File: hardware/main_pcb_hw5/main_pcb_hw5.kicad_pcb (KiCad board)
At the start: 2 copper layers, 100 x 100 mm, 27 parts, among them J1 MEGA TOP, J10 GBA_Slot, J2 MEGA BOTTOM, J3 CART SLOT TOP ROW, J4 CART SLOT BOTTOM ROW, J5 MEGA SIDE, J6 5V USB, J7 Conn_01x07, J8 EXP2, J9 EXP1, M2_1 Screw_Terminal_01x01, M2_2 Screw_Terminal_01x01, M2_3 Screw_Terminal_01x01, M2_4 Screw_Terminal_01x01, M2_5 Screw_Terminal_01x01, M2_6 Screw_Terminal_01x01, M2_7 Screw_Terminal_01x01, M2_8 Screw_Terminal_01x01, M2_9 Screw_Terminal_01x01, SW1 VOLTAGE, SW2 POWER

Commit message: Update silkscreen
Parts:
- JP2: value powered by 5V -> Testpoints 1 2
- JP3: value 3V3 from Arduino -> Testpoints 3 4
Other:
- board text added: "J1"
- board text added: "J2"
- board text added: "TP1"
- board text added: "TP2"
- board text added: "TP3"
- board text added: "TP4"
- board text removed: "powered by 5V"
- board text removed: "powered by VCC"
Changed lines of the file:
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@@
       (effects (font (size 1 1) (thickness 0.15)) (justify mirror))
     )
-    (fp_text value "powered by 5V" (at 5.01 -2.34 180 unlocked) (layer "B.SilkS") hide
+    (fp_text value "Testpoints 1 2" (at 5.01 -2.34 180 unlocked) (layer "B.SilkS") hide
       (effects (font (size 0.7 0.7) (thickness 0.15)) (justify left mirror))
     )
-    (fp_line (start -1.4 -1) (end -1.4 1) (layer "B.SilkS") (width 0.12))
-    (fp_line (start -1.4 1) (end 1.4 1) (layer "B.SilkS") (width 0.12))
-    (fp_line (start 1.4 1) (end 1.4 -1) (layer "B.SilkS") (width 0.12))
-    (fp_line (start 1.4 -1) (end -1.4 -1) (layer "B.SilkS") (width 0.12))
     (fp_line (start -1.65 1.25) (end 1.65 1.25) (layer "B.CrtYd") (width 0.05))
     (fp_line (start -1.65 1.25) (end -1.65 -1.25) (layer "B.CrtYd") (width 0.05))
     (fp_line (start 1.65 -1.25) (end -1.65 -1.25) (layer "B.CrtYd") (width 0.05))
     (fp_line (start 1.65 -1.25) (end 1.65 1.25) (layer "B.CrtYd") (width 0.05))
-    (pad "1" smd rect locked (at -0.65 0 180) (size 1 1.5) (layers "B.Cu" "B.Mask")
+    (pad "1" smd rect (at -0.65 0 180) (size 1 1.5) (layers "B.Cu" "B.Mask")
       (net 72 "+5V") (pinfunction "A") (pintype "passive"))
-    (pad "2" smd rect locked (at 0.65 0 180) (size 1 1.5) (layers "B.Cu" "B.Mask")
+    (pad "2" smd rect (at 0.65 0 180) (size 1 1.5) (layers "B.Cu" "B.Mask")
       (net 92 "VDDA") (pinfunction "B") (pintype "passive"))
   )
@@
       (effects (font (size 1 1) (thickness 0.15)) (justify mirror))
     )
-    (fp_text value "3V3 from Arduino" (at 11 0 180 unlocked) (layer "B.SilkS") hide
+    (fp_text value "Testpoints 3 4" (at 11 0 180 unlocked) (layer "B.SilkS") hide
       (effects (font (size 0.7 0.7) (thickness 0.15)) (justify left mirror))
     )
-    (fp_line (start -1.4 -1) (end -1.4 1) (layer "B.SilkS") (width 0.12))
-    (fp_line (start -1.4 1) (end 1.4 1) (layer "B.SilkS") (width 0.12))
-    (fp_line (start 1.4 -1) (end -1.4 -1) (layer "B.SilkS") (width 0.12))
-    (fp_line (start 1.4 1) (end 1.4 -1) (layer "B.SilkS") (width 0.12))
+    (fp_line (start 1.65 -1.25) (end -1.65 -1.25) (layer "B.CrtYd") (width 0.05))
+    (fp_line (start -1.65 1.25) (end -1.65 -1.25) (layer "B.CrtYd") (width 0.05))
+    (fp_line (start -1.65 1.25) (end 1.65 1.25) (layer "B.CrtYd") (width 0.05))
     (fp_line (start 1.65 -1.25) (end 1.65 1.25) (layer "B.CrtYd") (width 0.05))
-    (fp_line (start -1.65 1.25) (end 1.65 1.25) (layer "B.CrtYd") (width 0.05))
-    (fp_line (start -1.65 1.25) (end -1.65 -1.25) (layer "B.CrtYd") (width 0.05))
-    (fp_line (start 1.65 -1.25) (end -1.65 -1.25) (layer "B.CrtYd") (width 0.05))
-    (pad "1" smd rect locked (at -0.65 0 180) (size 1 1.5) (layers "B.Cu" "B.Mask")
+    (pad "1" smd rect (at -0.65 0 180) (size 1 1.5) (layers "B.Cu" "B.Mask")
       (net 35 "+3.3VA") (pinfunction "A") (pintype "passive"))
-    (pad "2" smd rect locked (at 0.65 0 180) (size 1 1.5) (layers "B.Cu" "B.Mask")
+    (pad "2" smd rect (at 0.65 0 180) (size 1 1.5) (layers "B.Cu" "B.Mask")
       (net 71 "+3V3") (pinfunction "B") (pintype "passive"))
   )
@@
   (gr_line (start 152.9063 146.1343) (end 152.8131 146.0411) (layer "B.SilkS") (width 0.1))
   (gr_line (start 138.7022 113.3433) (end 138.8887 113.3433) (layer "B.SilkS") (width 0.1))
-  (gr_line (start 169.21 123.505) (end 167.7 123.505) (layer "B.SilkS") (width 0.15))
   (gr_line (start 153.7874 143.5362) (end 154.1602 143.9091) (layer "B.SilkS") (width 0.1))
   (gr_line (start 154.1633 115.9735) (end 153.9769 115.9735) (layer "B.SilkS") (width 0.1))
@@
   (gr_line (start 110.97 115.68785) (end 110.5972 115.68785) (layer "B.SilkS") (width 0.1))
   (gr_line (start 152.9471 115.9735) (end 153.0403 115.8803) (layer "B.SilkS") (width 0.1))
-  (gr_line (start 170.35 121.43) (end 169.21 121.43) (layer "B.SilkS") (width 0.15))
   (gr_line (start 138.2671 115.4142) (end 137.8943 115.4142) (layer "B.SilkS") (width 0.1))
   (gr_line (start 115.2019 115.8836) (end 115.1087 115.9768) (layer "B.SilkS") (width 0.1))
@@
   (gr_line (start 132.6556 115.8803) (end 132.6556 115.5075) (layer "B.SilkS") (width 0.1))
   (gr_line (start 123.3135 146.0411) (end 123.1271 146.0411) (layer "B.SilkS") (width 0.1))
-  (gr_line (start 107.421 116.57) (end 107.611 116.81) (layer "B.SilkS") (width 0.15))
   (gr_line (start 143.8333 113.0637) (end 143.9265 113.0637) (layer "B.SilkS") (width 0.1))
   (gr_line (start 109.7534 113.33285) (end 109.567 113.33285) (layer "B.SilkS") (width 0.1))
@@
   (gr_line (start 117.6676 115.8803) (end 117.6676 115.5075) (layer "B.SilkS") (width 0.1))
   (gr_line (start 144.8851 143.9989) (end 145.1647 143.9989) (layer "B.SilkS") (width 0.1))
-  (gr_line (start 153.5 123.505) (end 107.42 123.505) (layer "B.SilkS") (width 0.15))
   (gr_line (start 146.4741 143.4397) (end 146.1013 143.4397) (layer "B.SilkS") (width 0.1))
   (gr_line (start 149.1178 115.5075) (end 149.0246 115.4142) (layer "B.SilkS") (width 0.1))
@@
   (gr_line (start 149.4548 138.1125) (end 150.0141 138.1125) (layer "B.SilkS") (width 0.1))
   (gr_line (start 133.778599 115.9735) (end 133.778599 115.4142) (layer "B.SilkS") (width 0.1))
-  (gr_line (start 169.21 125.58) (end 170.35 125.58) (layer "B.SilkS") (width 0.15))
   (gr_line (start 133.6005 113.1569) (end 133.414 113.0637) (layer "B.SilkS") (width 0.1))
   (gr_line (start 140.8546 146.414) (end 140.8546 146.5072) (layer "B.SilkS") (width 0.1))
@@
   (gr_line (start 138.8214 146.3208) (end 138.4485 146.3208) (layer "B.SilkS") (width 0.1))
   (gr_line (start 136.1541 143.9989) (end 135.9677 143.9989) (layer "B.SilkS") (width 0.1))
-  (gr_line (start 169.21 121.43) (end 169.21 125.58) (layer "B.SilkS") (width 0.15))
   (gr_line (start 140.1535 115.9735) (end 140.2467 115.8803) (layer "B.SilkS") (width 0.1))
   (gr_line (start 149.548 136.8963) (end 149.4548 136.8031) (layer "B.SilkS") (width 0.1))
@@
   (gr_line (start 147.4984 146.6004) (end 147.7781 146.6004) (layer "B.SilkS") (width 0.1))
   (gr_line (start 138.2133 146.1343) (end 138.2133 146.2276) (layer "B.SilkS") (width 0.1))
-  (gr_line (start 107.42 123.5) (end 107.42 116.57) (layer "B.SilkS") (width 0.15))
   (gr_line (start 135.6452 115.4142) (end 135.6452 115.9735) (layer "B.SilkS") (width 0.1))
   (gr_line (start 120.1343 112.7874) (end 119.8547 112.7874) (layer "B.SilkS") (width 0.1))
@@
   (gr_line (start 153.5552 115.4142) (end 153.6484 115.5075) (layer "B.SilkS") (width 0.1))
   (gr_line (start 134.6583 143.4397) (end 134.6583 143.9989) (layer "B.SilkS") (width 0.1))
-  (gr_line (start 107.421 116.57) (end 107.241 116.8) (layer "B.SilkS") (width 0.15))
   (gr_line (start 131.0464 143.4397) (end 131.1396 143.5329) (layer "B.SilkS") (width 0.1))
   (gr_line (start 120.5141 146.3241) (end 120.7937 146.6037) (layer "B.SilkS") (width 0.1))
@@
     (effects (font (size 0.7 0.7) (thickness 0.125)) (justify left mirror))
   )
+  (gr_text "TP2" (at 182.7 129 90) (layer "B.SilkS")
+    (effects (font (size 0.7 0.7) (thickness 0.125)) (justify right mirror))
+  )
   (gr_text "D4" (at 125.58 99.345 90) (layer "B.SilkS")
     (effects (font (size 0.7 0.7) (thickness 0.125)) (justify left mirror))
@@
     (effects (font (size 0.7 0.7) (thickness 0.125)) (justify left mirror))
   )
+  (gr_text "TP1" (at 181.4 129 90) (layer "B.SilkS")
+    (effects (font (size 0.7 0.7) (thickness 0.125)) (justify right mirror))
+  )
   (gr_text "D50" (at 194 83.935 90) (layer "B.SilkS")
     (effects (font (size 0.7 0.7) (thickness 0.125)) (justify left mirror))
@@
     (effects (font (size 0.7 0.7) (thickness 0.15)) (justify mirror))
   )
-  (gr_text "powered by 5V" (at 171.01 125.66 180) (layer "B.SilkS")
-    (effects (font (size 0.7 0.7) (thickness 0.125)) (justify left mirror))
-  )
   (gr_text "CLK1" (at 181.3 99.345 90) (layer "B.SilkS")
     (effects (font (size 0.7 0.7) (thickness 0.125)) (justify left mirror))
@@
     (effects (font (size 0.7 0.7) (thickness 0.125)) (justify left mirror))
   )
-  (gr_text "MEGA 2560 PRO" (at 154.24 123.5 180) (layer "B.SilkS")
-    (effects (font (size 1 1) (thickness 0.15)) (justify left mirror))
-  )
   (gr_text "CLK0" (at 181.3 114.415 180) (layer "B.SilkS")
     (effects (font (size 0.6 0.6) (thickness 0.15)) (justify mirror))
@@
     (effects (font (size 0.7 0.7) (thickness 0.125)) (justify left mirror))
   )
+  (gr_text "J1" (at 182.7 119.7 180) (layer "B.SilkS")
+    (effects (font (size 0.7 0.7) (thickness 0.125)) (justify right mirror))
+  )
   (gr_text "A12" (at 140.68 84.055 90) (layer "B.SilkS")
     (effects (font (size 0.7 0.7) (thickness 0.125)) (justify left mirror))
+  )
+  (gr_text "J2" (at 186.5 119.7 180) (layer "B.SilkS")
+    (effects (font (size 0.7 0.7) (thickness 0.125)) (justify right mirror))
   )
   (gr_text "D26" (at 143.36 99.345 90) (layer "B.SilkS")
@@
     (effects (font (size 0.7 0.7) (thickness 0.125)) (justify left mirror))
   )
+  (gr_text "TP3" (at 185.2 129 90) (layer "B.SilkS")
+    (effects (font (size 0.7 0.7) (thickness 0.125)) (justify right mirror))
+  )
   (gr_text "D28" (at 148.44 99.345 90) (layer "B.SilkS")
     (effects (font (size 0.7 0.7) (thickness 0.125)) (justify left mirror))
@@
     (effects (font (size 0.7 0.7) (thickness 0.125)) (justify left mirror))
   )
-  (gr_text "powered by VCC" (at 171.01 121.66 180) (layer "B.SilkS")
-    (effects (font (size 0.7 0.7) (thickness 0.125)) (justify left mirror))
-  )
   (gr_text "GND" (at 196.54 83.935 90) (layer "B.SilkS")
     (effects (font (size 0.7 0.7) (thickness 0.125)) (justify left mirror))
@@
     (effects (font (size 0.7 0.7) (thickness 0.125)) (justify left mirror))
   )
+  (gr_text "TP4" (at 186.6 129 90) (layer "B.SilkS")
+    (effects (font (size 0.7 0.7) (thickness 0.125)) (justify right mirror))
+  )
   (gr_text "D16" (at 173.7 84.055 90) (layer "B.SilkS")

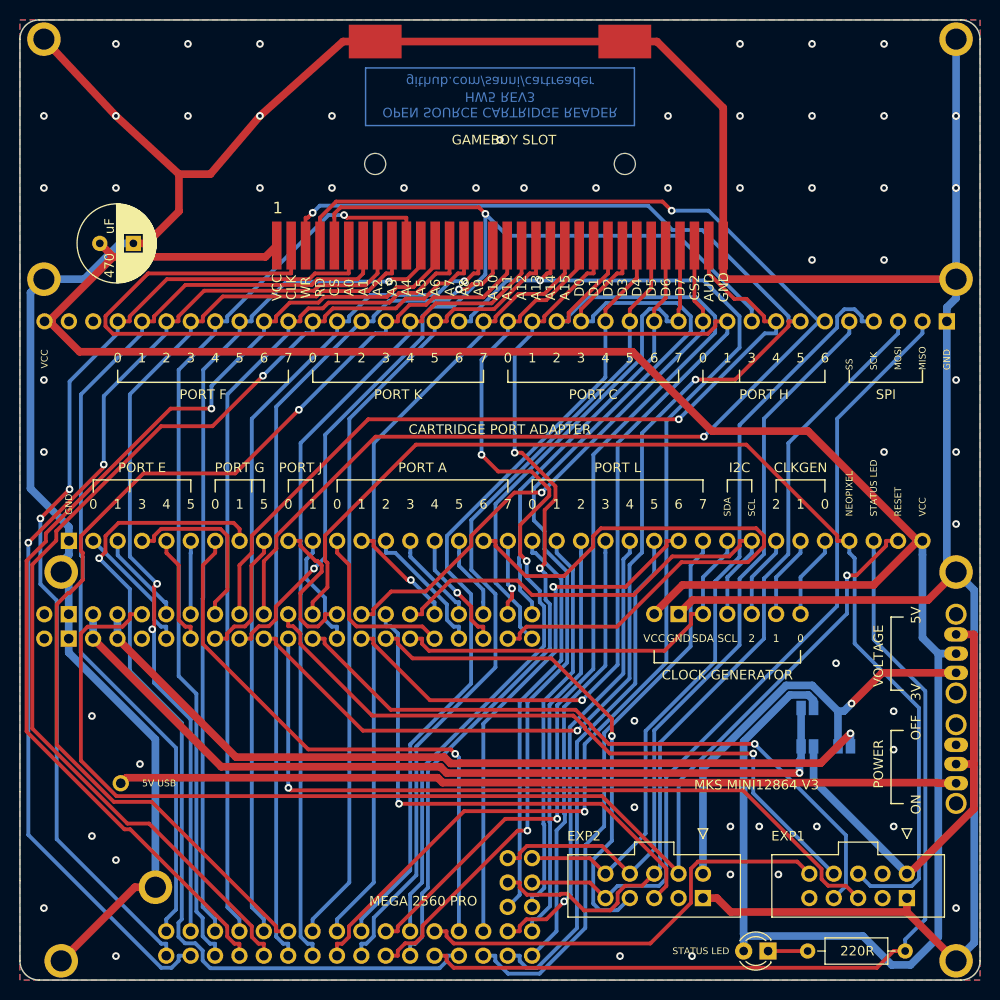
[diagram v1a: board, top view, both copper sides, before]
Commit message: New OSCR Logo + Vselect built into main PCB
Also added symbol and footprint library links
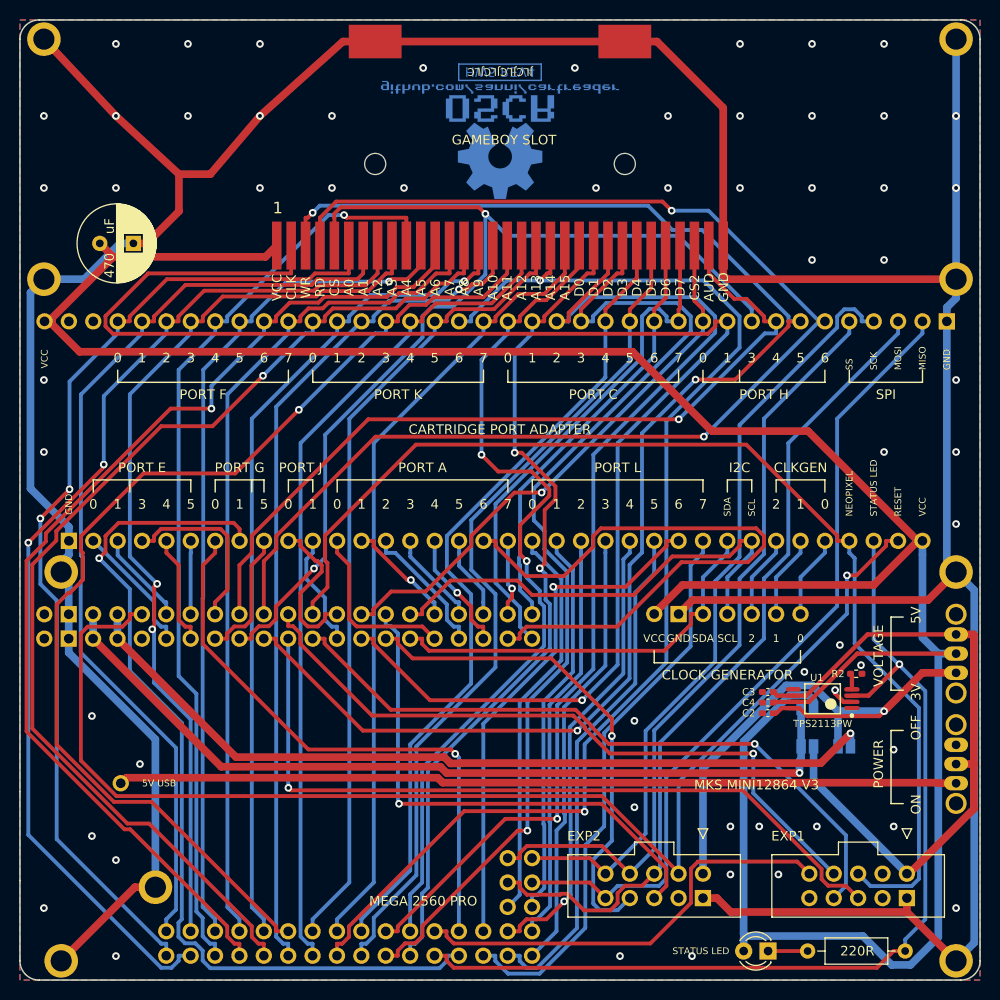
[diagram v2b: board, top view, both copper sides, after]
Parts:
- added C2: 0.1 uF, Capacitor_SMD:C_0402_1005Metric_Pad0.74x0.62mm_HandSolder, F.Cu at (177.9, 122.2)
- added C3: 0.1 uF, Capacitor_SMD:C_0402_1005Metric_Pad0.74x0.62mm_HandSolder, F.Cu at (177.9, 120.0)
- added C4: 10 uF, Capacitor_SMD:C_0402_1005Metric_Pad0.74x0.62mm_HandSolder, F.Cu at (177.9, 121.1)
- added G***: LOGO, !OSCR:Logo, B.Cu at (150.0, 62.5)
- added R2: 550, Resistor_SMD:R_0402_1005Metric_Pad0.72x0.64mm_HandSolder, F.Cu at (187.1, 118.1)
- added U1: TPS2113PW, Personal:Texas_Instruments-TPS2113PW-Level_A, F.Cu at (183.6, 120.7)
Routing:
- net +5V: track 48.9 -> 70.8 mm
- net VCC: track 259.2 -> 280.4 mm
- net +3V3: track 47.3 -> 59.6 mm
- net D38: track 96.4 -> 102.8 mm, vias 0 -> 1
- net GND: track 390.5 -> 392.9 mm, vias 58 -> 59
- net Net-(R2-Pad2): track 0.00 -> 1.69 mm
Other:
- board text added: "HW5 REV4"
- board text added: "JLCJLCJLCJLC"
- board text removed: "OPEN SOURCE CARTRIDGE READER HW5 REV3 github.com/sanni/cartreader"

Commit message: HW5 Main PCB, Revision 5
* Migrated files to KiCad 7
* Added RTC
  * IC: Analog Devices Inc. DS3231MZ
  * Battery holder (CR1616): Keystone Electronics 3012
* Cleaned up traces
* Changed ground fill to solid
* Removed test pads and LCD solder jumper
* Cleaned up/prettified silkscreen and logo
* Cleaned up some footprints (more to come eventually)
* Added 3D models for board display
* Schematic image is now a PDF since it has 2 pages
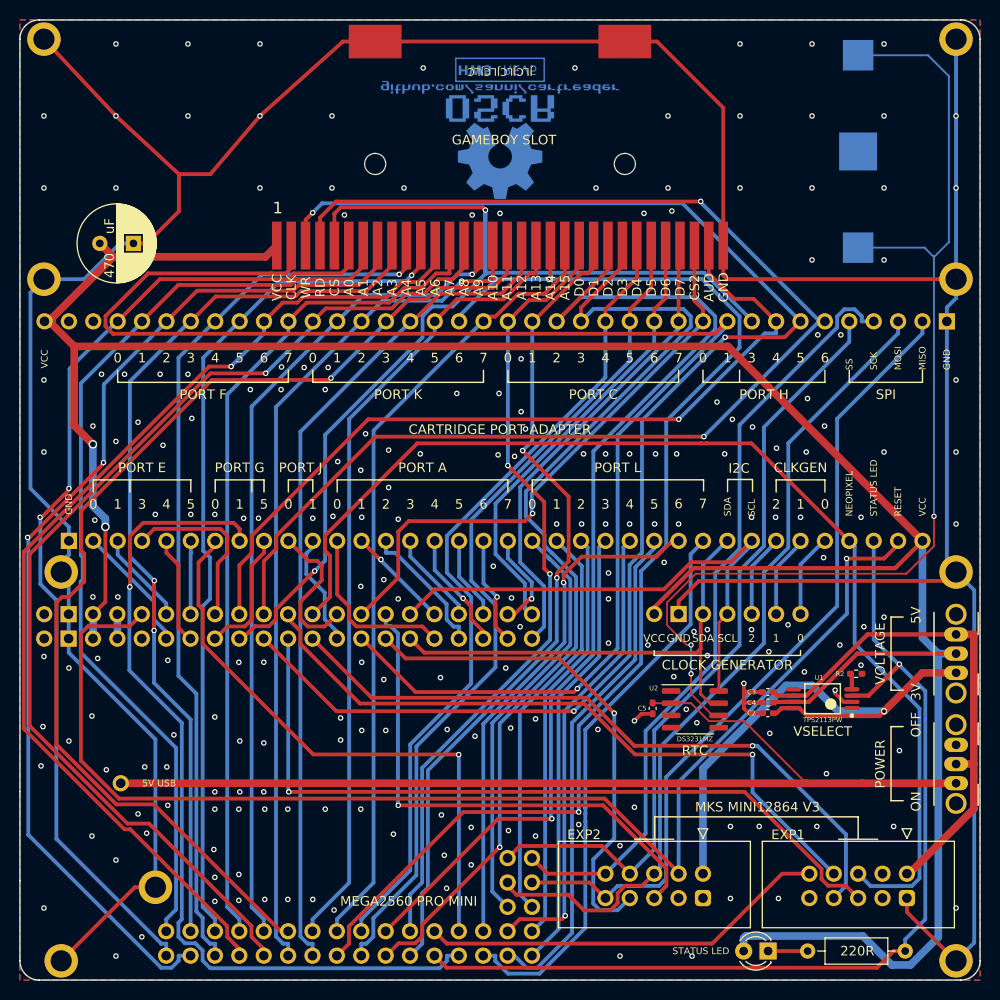
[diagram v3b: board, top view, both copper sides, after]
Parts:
- removed J2: MEGA BOTTOM, Connector_PinSocket_2.54mm:PinSocket_2x16_P2.54mm_Vertical
- removed J5: MEGA SIDE, Connector_PinSocket_2.54mm:PinSocket_2x03_P2.54mm_Vertical
- removed JP1: powered by VCC, Jumper:SolderJumper-2_P1.3mm_Open_Pad1.0x1.5mm
- removed JP2: Testpoints 1 2, Jumper:SolderJumper-2_P1.3mm_Open_Pad1.0x1.5mm
- removed JP3: Testpoints 3 4, Jumper:SolderJumper-2_P1.3mm_Open_Pad1.0x1.5mm
- added BT1: CR1616, !OSCR:CR1616, B.Cu at (187.3, 63.7)
- added C5: 0.1u, Capacitor_SMD:C_0402_1005Metric_Pad0.74x0.62mm_HandSolder, F.Cu at (165.9, 121.7)
- added U2: DS3231MZ, Package_SO:SOIC-8_3.9x4.9mm_P1.27mm, F.Cu at (170.3, 121.8)
- C1: value C_Polarized -> 470u
- C2, C3: value 0.1 uF -> 0.1u
- C4: value 10 uF -> 10u
- J1: value MEGA TOP -> MEGA BOTTOM; footprint Connector_PinSocket_2.54mm:PinSocket_2x21_P2.54mm_Vertical -> !OSCR:MEGA2560_PRO_MINI
- J3: footprint Connector_PinSocket_2.54mm:PinSocket_1x38_P2.54mm_Vertical -> !OSCR:Cartridge_Port_Adapter-Back
- J4: value CART SLOT BOTTOM ROW -> CART SLOT FRONT ROW; footprint Connector_PinSocket_2.54mm:PinSocket_1x36_P2.54mm_Vertical -> !OSCR:Cartridge_Port_Adapter-Front
- J7: footprint Connector_PinHeader_2.54mm:PinHeader_1x07_P2.54mm_Vertical -> !OSCR:Clock_Generator_Header
- J8, J9: footprint Connector_IDC:IDC-Header_2x05_P2.54mm_Vertical -> !OSCR:LCD_Header
- R2: value 550 -> 560R
- SW1, SW2: footprint Button_Switch_THT:SW_CuK_OS102011MA1QN1_SPDT_Angled -> !OSCR:Power_Switch
- moved J1 25.4 mm to (127.9, 113.0), turned to 0 degrees
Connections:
- J1 pad 37: VDDA -> VCC
- J1 pad 38: VDDA -> VCC
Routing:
- net +BATT: track 0.00 -> 113.2 mm, vias 0 -> 3
- net VDDA: track 88.7 -> 0.00 mm, vias 1 -> 0
- net +3.3VA: track 86.9 -> 2.54 mm, vias 1 -> 0
- net D28: track 66.1 -> 11.4 mm, vias 0 -> 1
- net VBUS: track 87.5 -> 106.5 mm
- net +5V: track 70.8 -> 53.5 mm
- net D20: track 42.2 -> 53.8 mm
- net GND: track 392.9 -> 382.8 mm, vias 59 -> 215
- net D37: track 90.0 -> 83.4 mm
- net D21: track 49.3 -> 55.8 mm
- net D30: track 54.4 -> 49.4 mm
- net D40: track 93.8 -> 89.7 mm
- net +3V3: track 59.6 -> 56.0 mm
- net D6: track 110.2 -> 113.6 mm
- net D39: track 46.0 -> 42.6 mm
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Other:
- rule pad_to_mask_clearance: 0 -> 0.05
- board text added: "3V3 5V"
- board text added: "HW5"
- board text added: "ON OFF"
- board text added: "REV${REVISION}"
- board text added: "RTC"
- board text added: "RTC BATTERY"
- board text added: "VSELECT"
- board text removed: "CLOCK GENERATOR"
- board text removed: "HW5 REV4"
- board text removed: "J1"
- board text removed: "J2"
- board text removed: "MEGA 2560 PRO"
- board text removed: "ON LCD"
- board text removed: "TP1"
- board text removed: "TP2"
- board text removed: "TP3"
- board text removed: "TP4"
